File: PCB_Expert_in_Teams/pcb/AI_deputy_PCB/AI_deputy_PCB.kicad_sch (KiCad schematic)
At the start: 23 parts, among them J1 Piezo Electric, J15 Conn_01x04_Socket, J3 Haptic Power and GND, J4 UART, J5 JST CONN from MCU, J6 JTAG, Q1 NMOS, U2 ESP32-WROOM-32UE

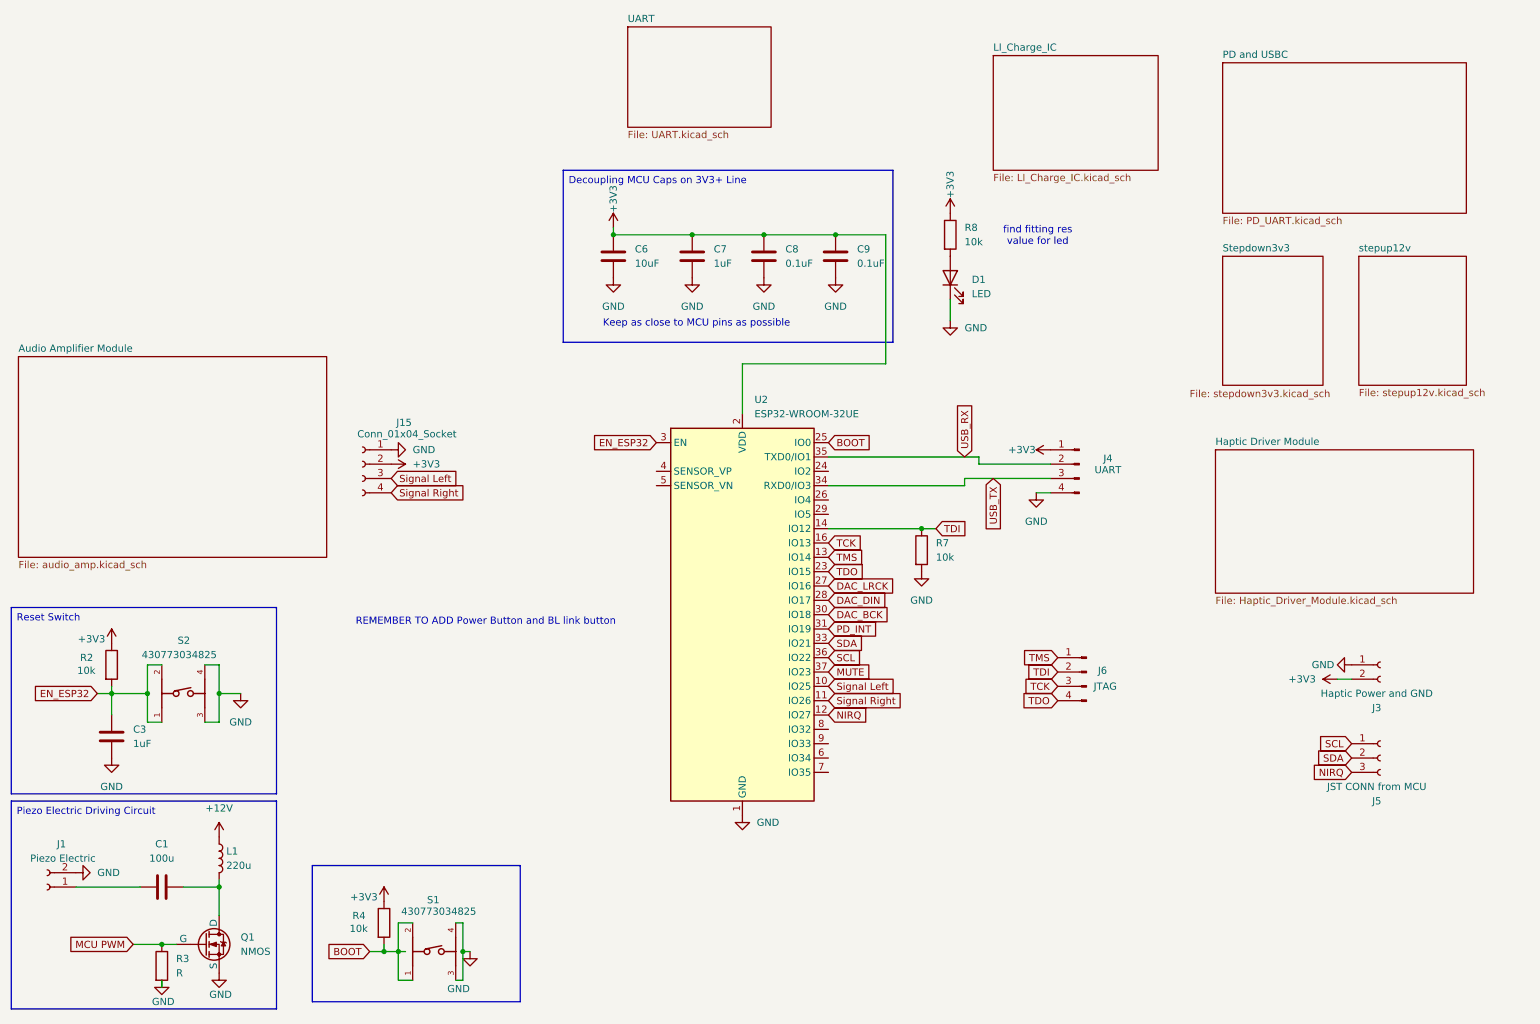
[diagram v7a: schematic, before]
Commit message: pcb updates from desktop with schematic fix
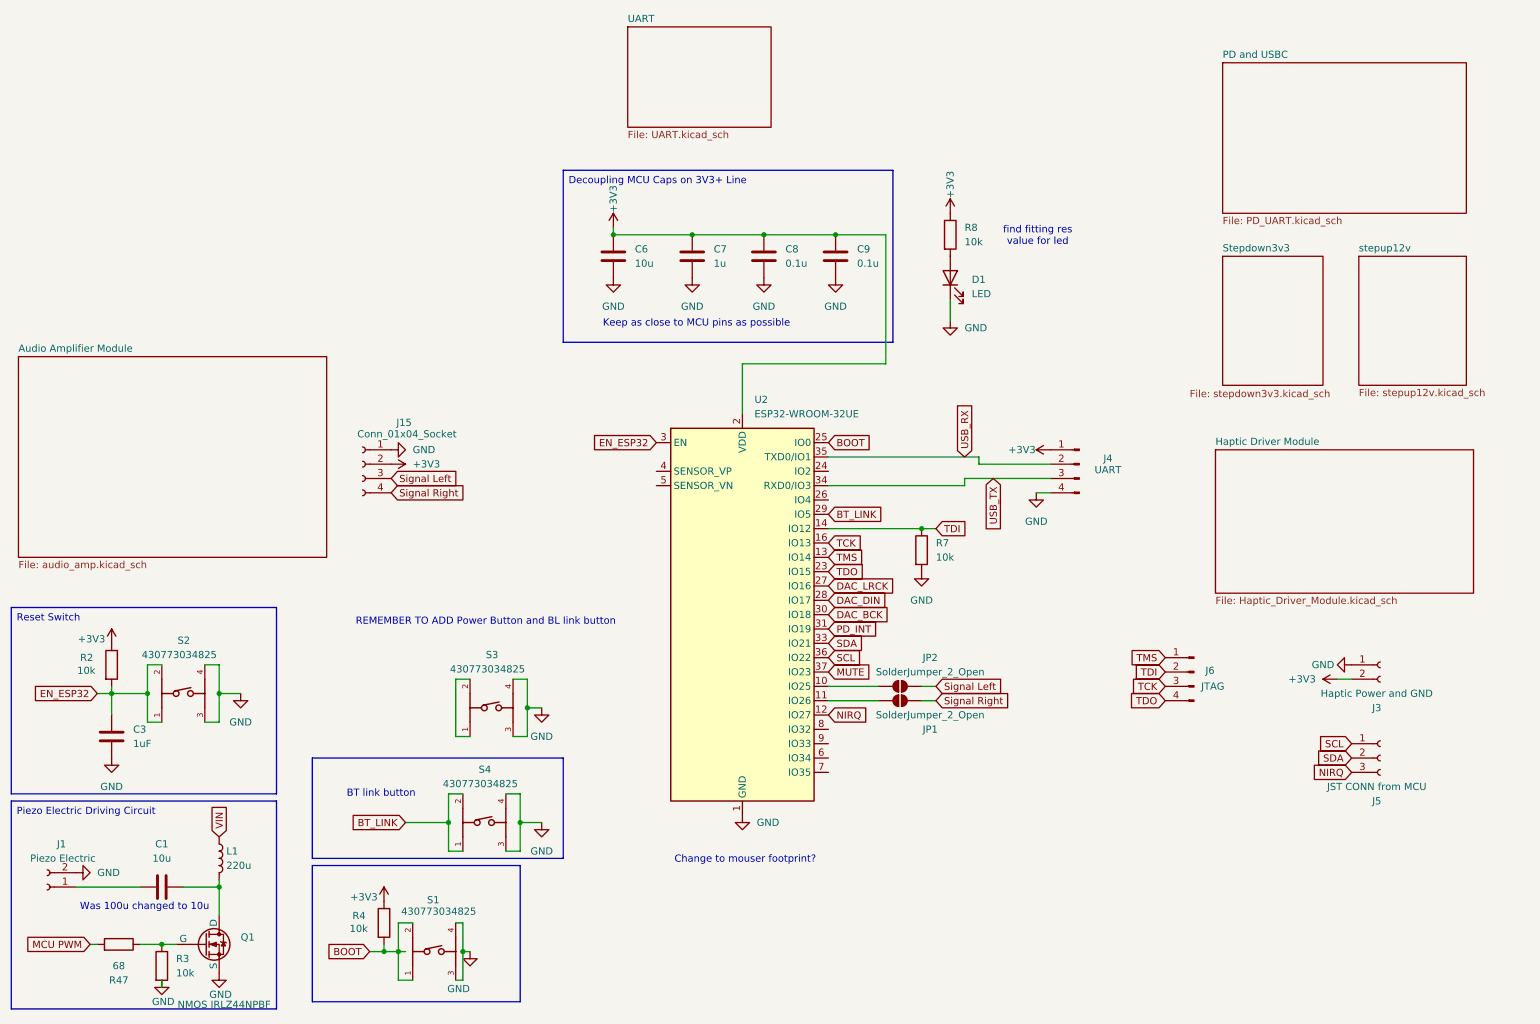
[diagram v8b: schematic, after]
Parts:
- added JP1, JP2: SolderJumper_2_Open, Jumper:SolderJumper-2_P1.3mm_Open_RoundedPad1.0x1.5mm, symbol Jumper:SolderJumper_2_Open
- added R47: 68, Resistor_SMD:R_0805_2012Metric_Pad1.20x1.40mm_HandSolder, symbol Device:R
- added S3, S4: 430773034825, EXT_AI_DEPUTY_Library:430773034825, symbol Wurth Buttons:430773034825
- C1: value 100u -> 10u
- C6: value 10uF -> 10u
- C7: value 1uF -> 1u
- C8, C9: value 0.1uF -> 0.1u
- Q1: value NMOS -> NMOS IRLZ44NPBF; footprint Package_TO_SOT_SMD:TO-252-3_TabPin2 -> Package_TO_SOT_THT:TO-220-3_Horizontal_TabDown
- R3: value R -> 10k
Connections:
- net GND: now also S3.3, S3.4, S4.3, S4.4
- net MCU PWM: now also R47.2; no longer Q1.2 (G), R3.1
- net Signal Left: now also JP2.2 (B); no longer U2.10 (IO25)
- net Signal Right: now also JP1.2 (B); no longer U2.11 (IO26)
- net BT_LINK: now reaches U2.29 (IO5)
- net BT_LINK: now also S4.1, S4.2
- net +12V renamed VIN
- new net: JP2.1 (A), U2.10 (IO25)
- new net: JP1.1 (A), U2.11 (IO26)
- new net: Q1.2 (G), R3.1, R47.1
- new net: S3.1, S3.2
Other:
- removed sheet LI_Charge_IC
- note added: "BT link button"
- note added: "Change to mouser footprint?"
- note added: "Was 100u changed to 10u"
- moved on the sheet: J6
